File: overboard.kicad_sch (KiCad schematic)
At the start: 243 parts, among them J1 USB_C_Receptacle_USB2.0, J2 Trackpoint, K1 Key_Switch_LED, K10 Key_Switch_LED, K11 Key_Switch_LED, K12 Key_Switch_LED, K13 Key_Switch_LED, K14 Key_Switch_LED, K15 Key_Switch_LED, K16 Key_Switch_LED, K17 Key_Switch_LED, K18 Key_Switch_LED, K19 Key_Switch_LED, K2 Key_Switch_LED, K20 Key_Switch_LED, K21 Key_Switch_LED, K22 Key_Switch_LED, K23 Key_Switch_LED, K24 Key_Switch_LED, K25 Key_Switch_LED, K26 Key_Switch_LED, K27 Key_Switch_LED, K28 Key_Switch_LED, K29 Key_Switch_LED, K3 Key_Switch_LED, K30 Key_Switch_LED, K31 Key_Switch_LED, K32 Key_Switch_LED, K33 Key_Switch_LED, K34 Key_Switch_LED, K35 Key_Switch_LED, K36 Key_Switch_LED, K37 Key_Switch_LED, K38 Key_Switch_LED, K39 Key_Switch_LED, K4 Key_Switch_LED, K40 Key_Switch_LED, K41 Key_Switch_LED, K42 Key_Switch_LED, K43 Key_Switch_LED, K44 Key_Switch_LED, K45 Key_Switch_LED, K46 Key_Switch_LED, K47 Key_Switch_LED, K48 Key_Switch_LED, K49 Key_Switch, K5 Key_Switch_LED, K50 Key_Switch, K51 Key_Switch, K6 Key_Switch_LED, K7 Key_Switch_LED, K8 Key_Switch_LED, K9 Key_Switch_LED, Q1 Q_NMOS_DGS, Q2 Q_NPN_Darlington_BCE, Q3 Q_NPN_Darlington_BCE, SW1 SW_DIP_x04, SW2 RotaryEncoder_Switch, SW3 RotaryEncoder_Switch, SW4 SW_Push, U1 Teensy2.0++, U2 SKQUCAA010, U3 SKQUCAA010

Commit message: Changes
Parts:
- removed K1, K10, K11, K12, K13, K14, K15, K16, K17, K18, K19, K2, K20, K21, K22, K23, K24, K25, K26, K27, K28, K29, K3, K30, K31, K32, K33, K34, K35, K36, K37, K38, K39, K4, K40, K41, K42, K43, K44, K45, K46, K47, K48, K5, K6, K7, K8, K9: Key_Switch_LED, LED_THT:LED_D1.8mm_W3.3mm_H2.4mm, symbol MK:Key_Switch_LED
- removed SW1: SW_DIP_x04, Package_DIP:DIP-4_W10.16mm, symbol Switch:SW_DIP_x04
- added D49, D50, D51, D52, D53, D54, D55, D56, D57, D58, D59, D60, D61, D62, D63, D64, D65, D66, D67, D68, D69, D70, D71, D72, D73, D74, D75, D76, D77, D78, D79, D80, D81, D82, D83, D84, D85, D86, D87, D88, D89, D90, D91, D92, D93, D94, D95, D96: LED, LED_THT:LED_D1.8mm_W3.3mm_H2.4mm, symbol Device:LED
- added J1: Pimoroni_Trackball, Kicad-Footprints:pimoroni_trackball, symbol User:Pimoroni_Trackball
- added K1, K10, K11, K12, K13, K14, K15, K16, K17, K18, K19, K2, K20, K21, K22, K23, K24, K25, K26, K27, K28, K29, K3, K30, K31, K32, K33, K34, K35, K36, K37, K38, K39, K4, K40, K41, K42, K43, K44, K45, K46, K47, K48, K5, K6, K7, K8, K9: Key_Switch, Switch_Keyboard_Hotswap_Kailh:SW_Hotswap_Kailh_MX_1.00u, symbol MK:Key_Switch
- added S1, S2: DS04-254-1L-02BK, DS04-254-1L-02BK:SW_DS04-254-1L-02BK, symbol DS04-254-1L-02BK:DS04-254-1L-02BK
- C1: footprint Capacitor_THT:CP_Radial_Tantal_D4.5mm_P2.50mm -> Capacitor_THT:CP_Radial_D5.0mm_P2.00mm
- J3: renamed from J1; footprint LED_THT:LED_D1.8mm_W3.3mm_H2.4mm -> Connector_USB:USB_C_Receptacle_HRO_TYPE-C-31-M-12
- K49, K50, K51: footprint Switch_Keyboard_Hotswap_Kailh:SW_Hotswap_Kailh_MX_1.00u -> Button_Switch_Keyboard:SW_Cherry_MX_1.00u_PCB
- L1, L2: footprint Inductor_THT:L_Axial_L5.3mm_D2.2mm_P2.54mm_Vertical_Vishay_IM-1 -> Connector_JST:JST_PH_S2B-PH-SM4-TB_1x02-1MP_P2.00mm_Horizontal
- LCD1: footprint Keebio-Parts:Resistor -> Display_0xLib:OLED_I2C_128x64_0.96inch
- LS1, LS2: footprint Keebio-Parts:Resistor -> Buzzer_Beeper:Buzzer_Mallory_AST1109MLTRQ
- Q1, Q2, Q3: footprint Keebio-Parts:Resistor -> digikey-footprints:TO-220-3
- SW3: renamed from SW4; footprint Button_Switch_THT:SW_PUSH_6mm -> User:Bourns 7914H; symbol Switch:SW_Push -> Switch:SW_SPST
- renumbered D49 to D1, D58 to D10, D4 to D100, D5 to D101, D6 to D102, D7 to D103, D8 to D104, D9 to D105, D10 to D106, D11 to D107, D12 to D108, D13 to D109, D59 to D11, D14 to D110, D15 to D111, D16 to D112, D17 to D113, D18 to D114, D19 to D115, D20 to D116, D21 to D117, D22 to D118, D23 to D119, D60 to D12, D24 to D120, D25 to D121, D26 to D122, D27 to D123, D28 to D124, D29 to D125, D30 to D126, D31 to D127, D32 to D128, D33 to D129, D61 to D13, D34 to D130, D35 to D131, D36 to D132, D37 to D133, D38 to D134, D39 to D135, D40 to D136, D41 to D137, D42 to D138, D43 to D139, D62 to D14, D44 to D140, D45 to D141, D46 to D142, D47 to D143, D48 to D144, D99 to D145, D107 to D146, D102 to D147, D109 to D148, D97 to D149, D63 to D15, D98 to D150, D103 to D151, D104 to D152, D108 to D153, D100 to D154, D101 to D155, D105 to D156, D106 to D157, D110 to D158, D111 to D159, D64 to D16, D112 to D160, D113 to D161, D114 to D162, D115 to D163, D116 to D164, D117 to D165, D65 to D17, D66 to D18, D67 to D19, D50 to D2, D68 to D20, D69 to D21, D70 to D22, D71 to D23, D72 to D24, D73 to D25, D74 to D26, D75 to D27, D76 to D28, D77 to D29, D51 to D3, D78 to D30, D79 to D31, D80 to D32, D81 to D33, D82 to D34, D83 to D35, D84 to D36, D85 to D37, D86 to D38, D87 to D39, D52 to D4, D88 to D40, D89 to D41, D90 to D42, D91 to D43, D92 to D44, D93 to D45, D94 to D46, D95 to D47, D96 to D48, D53 to D5, D54 to D6, D55 to D7, D56 to D8, D57 to D9, D1 to D97, D2 to D98, D3 to D99, R15 to R1, R17 to R15, R18 to R16, R19 to R17, R20 to R18, R21 to R19, R16 to R2, R22 to R20, R23 to R21, R24 to R22, R25 to R23, R26 to R24, R27 to R25, R28 to R26, R29 to R27, R30 to R28, R31 to R29, R32 to R30, R33 to R31, R34 to R32, R35 to R33, R36 to R34, R37 to R35, R38 to R36, R39 to R37, R40 to R38, R41 to R39, R42 to R40, R43 to R41, R44 to R42, R45 to R43, R46 to R44, R47 to R45, R48 to R46, R49 to R47, R50 to R48, R51 to R49, R52 to R50, R55 to R51, R56 to R52, R57 to R53, R1 to R54, R2 to R55, R53 to R56, R54 to R57, SW2 to SW1, SW3 to SW2
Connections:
- net COL0: now also K1.1, K13.1, K25.1, K37.1
- net COL1: now also K14.1, K2.1, K26.1, K38.1
- net COL10: now also K19.1, K31.1, K43.1, K7.1
- net COL11: now also K20.1, K32.1, K44.1, K8.1
- net COL12: now also K21.1, K33.1, K45.1, K9.1
- net COL13: now also K10.1, K22.1, K34.1, K46.1
- net COL14: now also K11.1, K23.1, K35.1, K47.1
- net COL15: now also K12.1, K24.1, K36.1, K48.1
- net COL2: now also K15.1, K27.1, K3.1, K39.1
- net COL3: now also K16.1, K28.1, K4.1, K40.1
- net COL4: now also K17.1, K29.1, K41.1, K5.1
- net COL5: now also K18.1, K30.1, K42.1, K6.1
- net COL6: now also S1.1B, S1.2B, S2.1B, S2.2B; no longer U2.4 (Com)
- net COL7: now also K49.1, K50.1, K51.1, SW1.S1, SW2.S1
- net COL8: now also U2.4 (Com); no longer U3.4 (Com)
- net COL9: now also U3.4 (Com); no longer K49.1, K50.1, K51.1, SW1.S1, SW2.S1
- net GND: now also J1.5 (GND)
- net SCL: now also J1.3 (SCL)
- net SDA: now also J1.2 (SDA)
- net VCC: now also D49.2 (A), D50.2 (A), D51.2 (A), D52.2 (A), D53.2 (A), D54.2 (A), D55.2 (A), D56.2 (A), D57.2 (A), D58.2 (A), D59.2 (A), D60.2 (A), D61.2 (A), D62.2 (A), D63.2 (A), D64.2 (A), D65.2 (A), D66.2 (A), D67.2 (A), D68.2 (A), D69.2 (A), D70.2 (A), D71.2 (A), D72.2 (A), D73.2 (A), D74.2 (A), D75.2 (A), D76.2 (A), D77.2 (A), D78.2 (A), D79.2 (A), D80.2 (A), D81.2 (A), D82.2 (A), D83.2 (A), D84.2 (A), D85.2 (A), D86.2 (A), D87.2 (A), D88.2 (A), D89.2 (A), D90.2 (A), D91.2 (A), D92.2 (A), D93.2 (A), D94.2 (A), D95.2 (A), D96.2 (A), J1.1 (VCC)
- net at D8.2 (A): now also K8.2
- net at D25.2 (A): now also K25.2
- net at R41.1: now also D87.1 (K)
- net at R20.1: now also D66.1 (K)
- net at D47.2 (A): now also K47.2
- net at R3.1: now also D49.1 (K)
- net at D48.2 (A): now also K48.2
- net at R33.1: now also D79.1 (K)
- net at R11.1: now also D57.1 (K)
- net at D33.2 (A): now also K33.2
- net at R37.1: now also D83.1 (K)
- net at R26.1: now also D72.1 (K)
- net at R8.1: now also D54.1 (K)
- net at D28.2 (A): now also K28.2
- net at D1.2 (A): now also K1.2
- net at D42.2 (A): now also K42.2
- net at D5.2 (A): now also K5.2
- net at D15.2 (A): now also K15.2
- net at D40.2 (A): now also K40.2
- net at R36.1: now also D82.1 (K)
- net at D6.2 (A): now also K6.2
- net at R17.1: now also D63.1 (K)
- net at R34.1: now also D80.1 (K)
- net at D20.2 (A): now also K20.2
- net at D148.2 (A): now also S2.2A
- net at D39.2 (A): now also K39.2
- net at D17.2 (A): now also K17.2
- net at D11.2 (A): now also K11.2
- net at D4.2 (A): now also K4.2
- net at D7.2 (A): now also K7.2
- net at D32.2 (A): now also K32.2
- net at R24.1: now also D70.1 (K)
- net at D41.2 (A): now also K41.2
- net at R4.1: now also D50.1 (K)
- net at R10.1: now also D56.1 (K)
- net at D146.2 (A): now also S2.1A
- net at D24.2 (A): now also K24.2
- net at R7.1: now also D53.1 (K)
- net at D44.2 (A): now also K44.2
- net at R31.1: now also D77.1 (K)
- net at D43.2 (A): now also K43.2
- net at R45.1: now also D91.1 (K)
- net at D34.2 (A): now also K34.2
- net at R49.1: now also D95.1 (K)
- net at R39.1: now also D85.1 (K)
- net at R48.1: now also D94.1 (K)
- net at D36.2 (A): now also K36.2
- net at D18.2 (A): now also K18.2
- net at D31.2 (A): now also K31.2
- net at R21.1: now also D67.1 (K)
- net at R16.1: now also D62.1 (K)
- net at R40.1: now also D86.1 (K)
- net at D26.2 (A): now also K26.2
- net at D2.2 (A): now also K2.2
- net at R47.1: now also D93.1 (K)
- net at D12.2 (A): now also K12.2
- net at R43.1: now also D89.1 (K)
- net at D9.2 (A): now also K9.2
- net at R5.1: now also D51.1 (K)
- net at R14.1: now also D60.1 (K)
- net at D45.2 (A): now also K45.2
- net at D16.2 (A): now also K16.2
- net at R28.1: now also D74.1 (K)
- net at R6.1: now also D52.1 (K)
- net at R27.1: now also D73.1 (K)
- net at D19.2 (A): now also K19.2
- net at R44.1: now also D90.1 (K)
- net at D38.2 (A): now also K38.2
- net at R32.1: now also D78.1 (K)
- net at R38.1: now also D84.1 (K)
- net at D10.2 (A): now also K10.2
- net at R29.1: now also D75.1 (K)
- net at R19.1: now also D65.1 (K)
- net at D27.2 (A): now also K27.2
- net at D23.2 (A): now also K23.2
- net at D30.2 (A): now also K30.2
- net at R23.1: now also D69.1 (K)
- net at R35.1: now also D81.1 (K)
- net at R46.1: now also D92.1 (K)
- net at D21.2 (A): now also K21.2
- net at D14.2 (A): now also K14.2
- net at D37.2 (A): now also K37.2
- net at R22.1: now also D68.1 (K)
- net at D13.2 (A): now also K13.2
- net at D3.2 (A): now also K3.2
- net at D22.2 (A): now also K22.2
- net at R42.1: now also D88.1 (K)
- net at D35.2 (A): now also K35.2
- net at D46.2 (A): now also K46.2
- net at D29.2 (A): now also K29.2
- net at R13.1: now also D59.1 (K)
- net at R50.1: now also D96.1 (K)
- net at R15.1: now also D61.1 (K)
- net at D145.2 (A): now also S1.1A
- net at R30.1: now also D76.1 (K)
- net at R12.1: now also D58.1 (K)
- net at R9.1: now also D55.1 (K)
- net at D147.2 (A): now also S1.2A
- net at R25.1: now also D71.1 (K)
- net at R18.1: now also D64.1 (K)
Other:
- moved on the sheet: C1, D1, D10, D100, D101, D102, D103, D104, D105, D106, D107, D108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

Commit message: Add USB-C port
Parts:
- removed D145, D146, D147, D148, D149, D150, D151, D152, D153, D154, D155, D156, D157, D158: 1N4148, Diode_THT:D_DO-35_SOD27_P7.62mm_Horizontal, symbol Diode:1N4148
- removed D49, D50, D51, D52, D53, D54, D55, D56, D57, D61, D62, D63, D64, D65, D66, D67, D68, D69, D70, D71, D72, D73, D74, D75, D76, D77, D78, D79, D80, D81, D82, D83, D84, D85, D86, D87, D88, D89, D90, D91, D92, D93, D94, D95, D96: LED, LED_THT:LED_D1.8mm_W3.3mm_H2.4mm, symbol Device:LED
- removed J1: Pimoroni_Trackball, Kicad-Footprints:pimoroni_trackball, symbol User:Pimoroni_Trackball
- removed J3: USB_C_Receptacle_USB2.0, Connector_USB:USB_C_Receptacle_HRO_TYPE-C-31-M-12, symbol Connector:USB_C_Receptacle_USB2.0
- removed LS2: AST1109MLTRQ, Buzzer_Beeper:Buzzer_Mallory_AST1109MLTRQ, symbol AST1109MLTRQ:AST1109MLTRQ
- removed R10, R11, R15, R16, R17, R18, R19, R20, R21, R22, R23, R24, R25, R26, R27, R28, R29, R3, R30, R31, R32, R33, R34, R35, R36, R37, R38, R39, R4, R40, R41, R42, R43, R44, R45, R46, R47, R48, R49, R5, R50, R6, R7, R8, R9: 470, Keebio-Parts:Resistor, symbol Device:R_Small_US
- removed R54, R55: 5.1k, Keebio-Parts:Resistor, symbol Device:R_Small_US
- removed S1, S2: DS04-254-1L-02BK, DS04-254-1L-02BK:SW_DS04-254-1L-02BK, symbol DS04-254-1L-02BK:DS04-254-1L-02BK
- removed SW3: SW_Push, User:Bourns 7914H, symbol Switch:SW_SPST
- removed U2, U3: SKQUCAA010, Alps SKQUCAA010:SKQUCAA010, symbol Alps SKQUCAA010:SKQUCAA010
- added D60, D61, D62, D63, D64, D70, D71, D72, D73, D80, D81, D82, D83, D84: 1N4148, Diode_SMD:D_SOD-123, symbol Diode:1N4148
- added DIP1: DS04-254-1L-04BK, DS04-254-1L-04BK:SW_DS04-254-1L-04BK, symbol DS04-254-1L-04BK:DS04-254-1L-04BK
- added H1, H2, H3, H4: MountingHole, User:MountingHole_2.4mm_M2, symbol Mechanical:MountingHole
- added H5: MountingHole, User:Trackpoint_Mounting_Holes, symbol Mechanical:MountingHole
- added J1: USB_C_Receptacle_USB2.0, USB_Type-C:USB_C_Receptacle_HRO_TYPE-C-31-M-12, symbol Connector:USB_C_Receptacle_USB2.0
- added J2: Conn_01x04, symbol Connector_Generic:Conn_01x04
- added NAV1, NAV2: JOYSTICK_MINI, Sparkfun_Switches:JOYSTICK_MINI, symbol Sparkfun_Switches:JOYSTICK_MINI
- added R1, R2: 5.1k, Keebio-Parts:Resistor, symbol Device:R_Small_US
- added SW1: Reset_SW, truckpoint:CK_RKB2_Switch, symbol Switch:SW_Push
- C1: footprint Capacitor_THT:CP_Radial_D5.0mm_P2.00mm -> Capacitor_THT:C_Radial_D4.0mm_H7.0mm_P1.50mm
- D00: renamed from D1; footprint Diode_THT:D_DO-35_SOD27_P7.62mm_Horizontal -> User:Diode_THT
- D01: renamed from D13; footprint Diode_THT:D_DO-35_SOD27_P7.62mm_Horizontal -> User:Diode_THT
- D02: renamed from D25; footprint Diode_THT:D_DO-35_SOD27_P7.62mm_Horizontal -> User:Diode_THT
- D03: renamed from D37; footprint Diode_THT:D_DO-35_SOD27_P7.62mm_Horizontal -> User:Diode_THT
- D10: renamed from D2; footprint Diode_THT:D_DO-35_SOD27_P7.62mm_Horizontal -> User:Diode_THT
- D11: renamed from D14; footprint Diode_THT:D_DO-35_SOD27_P7.62mm_Horizontal -> User:Diode_THT
- D12: renamed from D26; footprint Diode_THT:D_DO-35_SOD27_P7.62mm_Horizontal -> User:Diode_THT
- D13: renamed from D38; footprint Diode_THT:D_DO-35_SOD27_P7.62mm_Horizontal -> User:Diode_THT
- D20: renamed from D3; footprint Diode_THT:D_DO-35_SOD27_P7.62mm_Horizontal -> User:Diode_THT
- D21: renamed from D15; footprint Diode_THT:D_DO-35_SOD27_P7.62mm_Horizontal -> User:Diode_THT
- D22: renamed from D27; footprint Diode_THT:D_DO-35_SOD27_P7.62mm_Horizontal -> User:Diode_THT
- D23: renamed from D39; footprint Diode_THT:D_DO-35_SOD27_P7.62mm_Horizontal -> User:Diode_THT
- D30: renamed from D4; footprint Diode_THT:D_DO-35_SOD27_P7.62mm_Horizontal -> User:Diode_THT
- D31: renamed from D16; footprint Diode_THT:D_DO-35_SOD27_P7.62mm_Horizontal -> User:Diode_THT
- D32: renamed from D28; footprint Diode_THT:D_DO-35_SOD27_P7.62mm_Horizontal -> User:Diode_THT
- D33: renamed from D40; footprint Diode_THT:D_DO-35_SOD27_P7.62mm_Horizontal -> User:Diode_THT
- D40: renamed from D5; footprint Diode_THT:D_DO-35_SOD27_P7.62mm_Horizontal -> User:Diode_THT
- D41: renamed from D17; footprint Diode_THT:D_DO-35_SOD27_P7.62mm_Horizontal -> User:Diode_THT
- D42: renamed from D29; footprint Diode_THT:D_DO-35_SOD27_P7.62mm_Horizontal -> User:Diode_THT
- D43: renamed from D41; footprint Diode_THT:D_DO-35_SOD27_P7.62mm_Horizontal -> User:Diode_THT
- D50: renamed from D6; footprint Diode_THT:D_DO-35_SOD27_P7.62mm_Horizontal -> User:Diode_THT
- D51: renamed from D18; footprint Diode_THT:D_DO-35_SOD27_P7.62mm_Horizontal -> User:Diode_THT
- D52: renamed from D30; footprint Diode_THT:D_DO-35_SOD27_P7.62mm_Horizontal -> User:Diode_THT
- D53: renamed from D42; footprint Diode_THT:D_DO-35_SOD27_P7.62mm_Horizontal -> User:Diode_THT
- D90: renamed from D161; footprint Diode_THT:D_DO-35_SOD27_P7.62mm_Horizontal -> User:Diode_THT
- D91: renamed from D162; footprint Diode_THT:D_DO-35_SOD27_P7.62mm_Horizontal -> User:Diode_THT
- D92: renamed from D163; footprint Diode_THT:D_DO-35_SOD27_P7.62mm_Horizontal -> User:Diode_THT
- D93: renamed from D164; footprint Diode_THT:D_DO-35_SOD27_P7.62mm_Horizontal -> User:Diode_THT
- D94: renamed from D165; footprint Diode_THT:D_DO-35_SOD27_P7.62mm_Horizontal -> User:Diode_THT
- DA0: renamed from D7; footprint Diode_THT:D_DO-35_SOD27_P7.62mm_Horizontal -> User:Diode_THT
- DA1: renamed from D19; footprint Diode_THT:D_DO-35_SOD27_P7.62mm_Horizontal -> User:Diode_THT
- DA2: renamed from D31; footprint Diode_THT:D_DO-35_SOD27_P7.62mm_Horizontal -> User:Diode_THT
- DA3: renamed from D43; footprint Diode_THT:D_DO-35_SOD27_P7.62mm_Horizontal -> User:Diode_THT
- DB0: renamed from D8; footprint Diode_THT:D_DO-35_SOD27_P7.62mm_Horizontal -> User:Diode_THT
- DB1: renamed from D20; footprint Diode_THT:D_DO-35_SOD27_P7.62mm_Horizontal -> User:Diode_THT
- DB2: renamed from D32; footprint Diode_THT:D_DO-35_SOD27_P7.62mm_Horizontal -> User:Diode_THT
- DB3: renamed from D44; footprint Diode_THT:D_DO-35_SOD27_P7.62mm_Horizontal -> User:Diode_THT
- DC0: renamed from D9; footprint Diode_THT:D_DO-35_SOD27_P7.62mm_Horizontal -> User:Diode_THT
- DC1: renamed from D21; footprint Diode_THT:D_DO-35_SOD27_P7.62mm_Horizontal -> User:Diode_THT
- DC2: renamed from D33; footprint Diode_THT:D_DO-35_SOD27_P7.62mm_Horizontal -> User:Diode_THT
- DC3: renamed from D45; footprint Diode_THT:D_DO-35_SOD27_P7.62mm_Horizontal -> User:Diode_THT
- DD0: renamed from D10; footprint Diode_THT:D_DO-35_SOD27_P7.62mm_Horizontal -> User:Diode_THT
- DD1: renamed from D22; footprint Diode_THT:D_DO-35_SOD27_P7.62mm_Horizontal -> User:Diode_THT
- DD2: renamed from D34; footprint Diode_THT:D_DO-35_SOD27_P7.62mm_Horizontal -> User:Diode_THT
- DD3: renamed from D46; footprint Diode_THT:D_DO-35_SOD27_P7.62mm_Horizontal -> User:Diode_THT
- DE0: renamed from D11; footprint Diode_THT:D_DO-35_SOD27_P7.62mm_Horizontal -> User:Diode_THT
- DE1: renamed from D23; footprint Diode_THT:D_DO-35_SOD27_P7.62mm_Horizontal -> User:Diode_THT
- DE2: renamed from D35; footprint Diode_THT:D_DO-35_SOD27_P7.62mm_Horizontal -> User:Diode_THT
- DE3: renamed from D47; footprint Diode_THT:D_DO-35_SOD27_P7.62mm_Horizontal -> User:Diode_THT
- DF0: renamed from D12; footprint Diode_THT:D_DO-35_SOD27_P7.62mm_Horizontal -> User:Diode_THT
- DF1: renamed from D24; footprint Diode_THT:D_DO-35_SOD27_P7.62mm_Horizontal -> User:Diode_THT
- DF2: renamed from D36; footprint Diode_THT:D_DO-35_SOD27_P7.62mm_Horizontal -> User:Diode_THT
- DF3: renamed from D48; footprint Diode_THT:D_DO-35_SOD27_P7.62mm_Horizontal -> User:Diode_THT
- DL1: renamed from D159; footprint Diode_THT:D_DO-41_SOD81_P10.16mm_Horizontal -> Diode_THT:D_DO-41_SOD81_P7.62mm_Horizontal
- DL2: renamed from D160; footprint Diode_THT:D_DO-41_SOD81_P10.16mm_Horizontal -> Diode_THT:D_DO-41_SOD81_P7.62mm_Horizontal
- ENC1: renamed from SW1; footprint Encoder:RollerEncoder_Panasonic_EVQWGD001 -> User:Panasonic_EVQ-WGD001_LargerCutout
- ENC2: renamed from SW2; footprint Encoder:RollerEncoder_Panasonic_EVQWGD001 -> User:Panasonic_EVQ-WGD001_LargerCutout
- J3: renamed from J2; footprint pierce:TRACKPOINT -> Connector_PinHeader_2.54mm:PinHeader_1x05_P2.54mm_Vertical
- K00: renamed from K1; footprint Switch_Keyboard_Hotswap_Kailh:SW_Hotswap_Kailh_MX_1.00u -> MK_Switches:MXOnly-1U-NoLED
- K01: renamed from K13; footprint Switch_Keyboard_Hotswap_Kailh:SW_Hotswap_Kailh_MX_1.00u -> MK_Switches:MXOnly-1U-NoLED
- K02: renamed from K25; footprint Switch_Keyboard_Hotswap_Kailh:SW_Hotswap_Kailh_MX_1.00u -> MK_Switches:MXOnly-1U-NoLED
- K03: renamed from K37; footprint Switch_Keyboard_Hotswap_Kailh:SW_Hotswap_Kailh_MX_1.00u -> MK_Switches:MXOnly-1U-NoLED
- K10: renamed from K2; footprint Switch_Keyboard_Hotswap_Kailh:SW_Hotswap_Kailh_MX_1.00u -> MK_Switches:MXOnly-1U-NoLED
- K11: renamed from K14; footprint Switch_Keyboard_Hotswap_Kailh:SW_Hotswap_Kailh_MX_1.00u -> MK_Switches:MXOnly-1U-NoLED
- K12: renamed from K26; footprint Switch_Keyboard_Hotswap_Kailh:SW_Hotswap_Kailh_MX_1.00u -> MK_Switches:MXOnly-1U-NoLED
- K13: renamed from K38; footprint Switch_Keyboard_Hotswap_Kailh:SW_Hotswap_Kailh_MX_1.00u -> MK_Switches:MXOnly-1U-NoLED
- K20: renamed from K3; footprint Switch_Keyboard_Hotswap_Kailh:SW_Hotswap_Kailh_MX_1.00u -> MK_Switches:MXOnly-1U-NoLED
- K21: renamed from K15; footprint Switch_Keyboard_Hotswap_Kailh:SW_Hotswap_Kailh_MX_1.00u -> MK_Switches:MXOnly-1U-NoLED
- K22: renamed from K27; footprint Switch_Keyboard_Hotswap_Kailh:SW_Hotswap_Kailh_MX_1.00u -> MK_Switches:MXOnly-1U-NoLED
- K23: renamed from K39; footprint Switch_Keyboard_Hotswap_Kailh:SW_Hotswap_Kailh_MX_1.00u -> MK_Switches:MXOnly-1U-NoLED
- K30: renamed from K4; footprint Switch_Keyboard_Hotswap_Kailh:SW_Hotswap_Kailh_MX_1.00u -> MK_Switches:MXOnly-1U-NoLED
- K31: renamed from K16; footprint Switch_Keyboard_Hotswap_Kailh:SW_Hotswap_Kailh_MX_1.00u -> MK_Switches:MXOnly-1U-NoLED
- K32: renamed from K28; footprint Switch_Keyboard_Hotswap_Kailh:SW_Hotswap_Kailh_MX_1.00u -> MK_Switches:MXOnly-1U-NoLED
- K33: renamed from K40; footprint Switch_Keyboard_Hotswap_Kailh:SW_Hotswap_Kailh_MX_1.00u -> MK_Switches:MXOnly-1U-NoLED
- K40: renamed from K5; footprint Switch_Keyboard_Hotswap_Kailh:SW_Hotswap_Kailh_MX_1.00u -> MK_Switches:MXOnly-1U-NoLED
- K41: renamed from K17; footprint Switch_Keyboard_Hotswap_Kailh:SW_Hotswap_Kailh_MX_1.00u -> MK_Switches:MXOnly-1U-NoLED
- K42: renamed from K29; footprint Switch_Keyboard_Hotswap_Kailh:SW_Hotswap_Kailh_MX_1.00u -> MK_Switches:MXOnly-1U-NoLED
- K43: renamed from K41; footprint Switch_Keyboard_Hotswap_Kailh:SW_Hotswap_Kailh_MX_1.00u -> MK_Switches:MXOnly-1U-NoLED
- K50: renamed from K6; footprint Switch_Keyboard_Hotswap_Kailh:SW_Hotswap_Kailh_MX_1.00u -> MK_Switches:MXOnly-1U-NoLED
- K51: renamed from K18; footprint Switch_Keyboard_Hotswap_Kailh:SW_Hotswap_Kailh_MX_1.00u -> MK_Switches:MXOnly-1U-NoLED
- K52: renamed from K30; footprint Switch_Keyboard_Hotswap_Kailh:SW_Hotswap_Kailh_MX_1.00u -> MK_Switches:MXOnly-1U-NoLED
- K53: renamed from K42; footprint Switch_Keyboard_Hotswap_Kailh:SW_Hotswap_Kailh_MX_1.00u -> MK_Switches:MXOnly-1U-NoLED
- K92: renamed from K49; footprint Button_Switch_Keyboard:SW_Cherry_MX_1.00u_PCB -> MK_Switches:MXOnly-1U-NoLED
- K93: renamed from K50; footprint Button_Switch_Keyboard:SW_Cherry_MX_1.00u_PCB -> MK_Switches:MXOnly-1U-NoLED
- K94: renamed from K51; footprint Button_Switch_Keyboard:SW_Cherry_MX_1.00u_PCB -> MK_Switches:MXOnly-1U-NoLED
- KA0: renamed from K7; footprint Switch_Keyboard_Hotswap_Kailh:SW_Hotswap_Kailh_MX_1.00u -> MK_Switches:MXOnly-1U-NoLED
- KA1: renamed from K19; footprint Switch_Keyboard_Hotswap_Kailh:SW_Hotswap_Kailh_MX_1.00u -> MK_Switches:MXOnly-1U-NoLED
- KA2: renamed from K31; footprint Switch_Keyboard_Hotswap_Kailh:SW_Hotswap_Kailh_MX_1.00u -> MK_Switches:MXOnly-1U-NoLED
- KA3: renamed from K43; footprint Switch_Keyboard_Hotswap_Kailh:SW_Hotswap_Kailh_MX_1.00u -> MK_Switches:MXOnly-1U-NoLED
- KB0: renamed from K8; footprint Switch_Keyboard_Hotswap_Kailh:SW_Hotswap_Kailh_MX_1.00u -> MK_Switches:MXOnly-1U-NoLED
- KB1: renamed from K20; footprint Switch_Keyboard_Hotswap_Kailh:SW_Hotswap_Kailh_MX_1.00u -> MK_Switches:MXOnly-1U-NoLED
- KB2: renamed from K32; footprint Switch_Keyboard_Hotswap_Kailh:SW_Hotswap_Kailh_MX_1.00u -> MK_Switches:MXOnly-1U-NoLED
- KB3: renamed from K44; footprint Switch_Keyboard_Hotswap_Kailh:SW_Hotswap_Kailh_MX_1.00u -> MK_Switches:MXOnly-1U-NoLED
- KC0: renamed from K9; footprint Switch_Keyboard_Hotswap_Kailh:SW_Hotswap_Kailh_MX_1.00u -> MK_Switches:MXOnly-1U-NoLED
- KC1: renamed from K21; footprint Switch_Keyboard_Hotswap_Kailh:SW_Hotswap_Kailh_MX_1.00u -> MK_Switches:MXOnly-1U-NoLED
- KC2: renamed from K33; footprint Switch_Keyboard_Hotswap_Kailh:SW_Hotswap_Kailh_MX_1.00u -> MK_Switches:MXOnly-1U-NoLED
- KC3: renamed from K45; footprint Switch_Keyboard_Hotswap_Kailh:SW_Hotswap_Kailh_MX_1.00u -> MK_Switches:MXOnly-1U-NoLED
- KD0: renamed from K10; footprint Switch_Keyboard_Hotswap_Kailh:SW_Hotswap_Kailh_MX_1.00u -> MK_Switches:MXOnly-1U-NoLED
- KD1: renamed from K22; footprint Switch_Keyboard_Hotswap_Kailh:SW_Hotswap_Kailh_MX_1.00u -> MK_Switches:MXOnly-1U-NoLED
- KD2: renamed from K34; footprint Switch_Keyboard_Hotswap_Kailh:SW_Hotswap_Kailh_MX_1.00u -> MK_Switches:MXOnly-1U-NoLED
- KD3: renamed from K46; footprint Switch_Keyboard_Hotswap_Kailh:SW_Hotswap_Kailh_MX_1.00u -> MK_Switches:MXOnly-1U-NoLED
- KE0: renamed from K11; footprint Switch_Keyboard_Hotswap_Kailh:SW_Hotswap_Kailh_MX_1.00u -> MK_Switches:MXOnly-1U-NoLED
- KE1: renamed from K23; footprint Switch_Keyboard_Hotswap_Kailh:SW_Hotswap_Kailh_MX_1.00u -> MK_Switches:MXOnly-1U-NoLED
- KE2: renamed from K35; footprint Switch_Keyboard_Hotswap_Kailh:SW_Hotswap_Kailh_MX_1.00u -> MK_Switches:MXOnly-1U-NoLED
- KE3: renamed from K47; footprint Switch_Keyboard_Hotswap_Kailh:SW_Hotswap_Kailh_MX_1.00u -> MK_Switches:MXOnly-1U-NoLED
- KF0: renamed from K12; footprint Switch_Keyboard_Hotswap_Kailh:SW_Hotswap_Kailh_MX_1.00u -> MK_Switches:MXOnly-1U-NoLED
- KF1: renamed from K24; footprint Switch_Keyboard_Hotswap_Kailh:SW_Hotswap_Kailh_MX_1.00u -> MK_Switches:MXOnly-1U-NoLED
- KF2: renamed from K36; footprint Switch_Keyboard_Hotswap_Kailh:SW_Hotswap_Kailh_MX_1.00u -> MK_Switches:MXOnly-1U-NoLED
- KF3: renamed from K48; footprint Switch_Keyboard_Hotswap_Kailh:SW_Hotswap_Kailh_MX_1.00u -> MK_Switches:MXOnly-1U-NoLED
- L1, L2: footprint Connector_JST:JST_PH_S2B-PH-SM4-TB_1x02-1MP_P2.00mm_Horizontal -> Connector_JST:JST_PH_S2B-PH-K_1x02_P2.00mm_Horizontal
- RGB1: renamed from D97; footprint LED_SMD_0xLib:LED_SK6812MINI-E_3.2x2.8mm -> User:SK6812MINI-E_RGB_LED_3.2x2.8mm
- RGB10: renamed from D111; footprint LED_SMD_0xLib:LED_SK6812MINI-E_3.2x2.8mm -> User:SK6812MINI-E_RGB_LED_3.2x2.8mm
- RGB11: renamed from D110; footprint LED_SMD_0xLib:LED_SK6812MINI-E_3.2x2.8mm -> User:SK6812MINI-E_RGB_LED_3.2x2.8mm
- RGB12: renamed from D109; footprint LED_SMD_0xLib:LED_SK6812MINI-E_3.2x2.8mm -> User:SK6812MINI-E_RGB_LED_3.2x2.8mm
- RGB13: renamed from D108; footprint LED_SMD_0xLib:LED_SK6812MINI-E_3.2x2.8mm -> User:SK6812MINI-E_RGB_LED_3.2x2.8mm
- RGB14: renamed from D107; footprint LED_SMD_0xLib:LED_SK6812MINI-E_3.2x2.8mm -> User:SK6812MINI-E_RGB_LED_3.2x2.8mm
- RGB15: renamed from D106; footprint LED_SMD_0xLib:LED_SK6812MINI-E_3.2x2.8mm -> User:SK6812MINI-E_RGB_LED_3.2x2.8mm
- RGB16: renamed from D105; footprint LED_SMD_0xLib:LED_SK6812MINI-E_3.2x2.8mm -> User:SK6812MINI-E_RGB_LED_3.2x2.8mm
- RGB17: renamed from D113; footprint LED_SMD_0xLib:LED_SK6812MINI-E_3.2x2.8mm -> User:SK6812MINI-E_RGB_LED_3.2x2.8mm
- RGB18: renamed from D114; footprint LED_SMD_0xLib:LED_SK6812MINI-E_3.2x2.8mm -> User:SK6812MINI-E_RGB_LED_3.2x2.8mm
- RGB19: renamed from D115; footprint LED_SMD_0xLib:LED_SK6812MINI-E_3.2x2.8mm -> User:SK6812MINI-E_RGB_LED_3.2x2.8mm
- RGB2: renamed from D98; footprint LED_SMD_0xLib:LED_SK6812MINI-E_3.2x2.8mm -> User:SK6812MINI-E_RGB_LED_3.2x2.8mm
- RGB20: renamed from D116; footprint LED_SMD_0xLib:LED_SK6812MINI-E_3.2x2.8mm -> User:SK6812MINI-E_RGB_LED_3.2x2.8mm
- RGB21: renamed from D117; footprint LED_SMD_0xLib:LED_SK6812MINI-E_3.2x2.8mm -> User:SK6812MINI-E_RGB_LED_3.2x2.8mm
- RGB22: renamed from D118; footprint LED_SMD_0xLib:LED_SK6812MINI-E_3.2x2.8mm -> User:SK6812MINI-E_RGB_LED_3.2x2.8mm
- RGB23: renamed from D119; footprint LED_SMD_0xLib:LED_SK6812MINI-E_3.2x2.8mm -> User:SK6812MINI-E_RGB_LED_3.2x2.8mm
- RGB24: renamed from D120; footprint LED_SMD_0xLib:LED_SK6812MINI-E_3.2x2.8mm -> User:SK6812MINI-E_RGB_LED_3.2x2.8mm
- RGB25: renamed from D128; footprint LED_SMD_0xLib:LED_SK6812MINI-E_3.2x2.8mm -> User:SK6812MINI-E_RGB_LED_3.2x2.8mm
- RGB26: renamed from D127; footprint LED_SMD_0xLib:LED_SK6812MINI-E_3.2x2.8mm -> User:SK6812MINI-E_RGB_LED_3.2x2.8mm
- RGB27: renamed from D126; footprint LED_SMD_0xLib:LED_SK6812MINI-E_3.2x2.8mm -> User:SK6812MINI-E_RGB_LED_3.2x2.8mm
- RGB28: renamed from D125; footprint LED_SMD_0xLib:LED_SK6812MINI-E_3.2x2.8mm -> User:SK6812MINI-E_RGB_LED_3.2x2.8mm
- RGB29: renamed from D124; footprint LED_SMD_0xLib:LED_SK6812MINI-E_3.2x2.8mm -> User:SK6812MINI-E_RGB_LED_3.2x2.8mm
- RGB3: renamed from D99; footprint LED_SMD_0xLib:LED_SK6812MINI-E_3.2x2.8mm -> User:SK6812MINI-E_RGB_LED_3.2x2.8mm
- RGB30: renamed from D123; footprint LED_SMD_0xLib:LED_SK6812MINI-E_3.2x2.8mm -> User:SK6812MINI-E_RGB_LED_3.2x2.8mm
- RGB31: renamed from D122; footprint LED_SMD_0xLib:LED_SK6812MINI-E_3.2x2.8mm -> User:SK6812MINI-E_RGB_LED_3.2x2.8mm
- RGB32: renamed from D121; footprint LED_SMD_0xLib:LED_SK6812MINI-E_3.2x2.8mm -> User:SK6812MINI-E_RGB_LED_3.2x2.8mm
- RGB33: renamed from D129; footprint LED_SMD_0xLib:LED_SK6812MINI-E_3.2x2.8mm -> User:SK6812MINI-E_RGB_LED_3.2x2.8mm
- RGB34: renamed from D130; footprint LED_SMD_0xLib:LED_SK6812MINI-E_3.2x2.8mm -> User:SK6812MINI-E_RGB_LED_3.2x2.8mm
- RGB35: renamed from D131; footprint LED_SMD_0xLib:LED_SK6812MINI-E_3.2x2.8mm -> User:SK6812MINI-E_RGB_LED_3.2x2.8mm
- RGB36: renamed from D132; footprint LED_SMD_0xLib:LED_SK6812MINI-E_3.2x2.8mm -> User:SK6812MINI-E_RGB_LED_3.2x2.8mm
- RGB37: renamed from D133; footprint LED_SMD_0xLib:LED_SK6812MINI-E_3.2x2.8mm -> User:SK6812MINI-E_RGB_LED_3.2x2.8mm
- RGB38: renamed from D134; footprint LED_SMD_0xLib:LED_SK6812MINI-E_3.2x2.8mm -> User:SK6812MINI-E_RGB_LED_3.2x2.8mm
- RGB39: renamed from D135; footprint LED_SMD_0xLib:LED_SK6812MINI-E_3.2x2.8mm -> User:SK6812MINI-E_RGB_LED_3.2x2.8mm
- RGB4: renamed from D100; footprint LED_SMD_0xLib:LED_SK6812MINI-E_3.2x2.8mm -> User:SK6812MINI-E_RGB_LED_3.2x2.8mm
- RGB40: renamed from D136; footprint LED_SMD_0xLib:LED_SK6812MINI-E_3.2x2.8mm -> User:SK6812MINI-E_RGB_LED_3.2x2.8mm
- RGB41: renamed from D144; footprint LED_SMD_0xLib:LED_SK6812MINI-E_3.2x2.8mm -> User:SK6812MINI-E_RGB_LED_3.2x2.8mm
- RGB42: renamed from D143; footprint LED_SMD_0xLib:LED_SK6812MINI-E_3.2x2.8mm -> User:SK6812MINI-E_RGB_LED_3.2x2.8mm
- RGB43: renamed from D142; footprint LED_SMD_0xLib:LED_SK6812MINI-E_3.2x2.8mm -> User:SK6812MINI-E_RGB_LED_3.2x2.8mm
- RGB44: renamed from D141; footprint LED_SMD_0xLib:LED_SK6812MINI-E_3.2x2.8mm -> User:SK6812MINI-E_RGB_LED_3.2x2.8mm
- RGB45: renamed from D140; footprint LED_SMD_0xLib:LED_SK6812MINI-E_3.2x2.8mm -> User:SK6812MINI-E_RGB_LED_3.2x2.8mm
- RGB46: renamed from D139; footprint LED_SMD_0xLib:LED_SK6812MINI-E_3.2x2.8mm -> User:SK6812MINI-E_RGB_LED_3.2x2.8mm
- RGB47: renamed from D138; footprint LED_SMD_0xLib:LED_SK6812MINI-E_3.2x2.8mm -> User:SK6812MINI-E_RGB_LED_3.2x2.8mm
- RGB48: renamed from D137; footprint LED_SMD_0xLib:LED_SK6812MINI-E_3.2x2.8mm -> User:SK6812MINI-E_RGB_LED_3.2x2.8mm
- renumbered D58 to LED1, D59 to LED2, D60 to LED3, LCD1 to OLED1, Q2 to Q1, Q3 to Q2, Q1 to Q3, R14 to R10, R13 to R11, R51 to R3, R53 to R4, R52 to R5, R56 to R6, R57 to R7, R1 to R8, R2 to R9
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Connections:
- net AUDIO: now also U1.19 (PC6_OC3A); no longer U1.17 (PC4_OC3C)
- net BACKLIGHT: now also U1.18 (PC5_OC3B); no longer U1.19 (PC6_OC3A)
- net COL0: no longer U1.41 (PB5_OC1A)
- net COL1: no longer U1.40 (PB4_OC2A)
- net COL2: no longer U1.39 (PB3_MISO)
- net COL3: no longer U1.38 (PB2_MOSI)
- net COL4: no longer U1.37 (PB1_SCLK)
- net COL5: no longer U1.36 (PB0_SS)
- net COL6: now also NAV1.GND; no longer U1.35 (PE7_INT7_AIN1)
- net COL7: now also DIP1.1A, DIP1.2A, DIP1.3A, DIP1.4A; no longer ENC1.S1, ENC2.S1, K92.1, K93.1, K94.1, U1.34 (PE6_INT6_AIN0)
- net COL8: now also NAV2.GND; no longer U1.31 (PF0_ADC0)
- net COL9: now also ENC1.S1, ENC2.S1, K92.1, K93.1, K94.1; no longer U1.30 (PF1_ADC1)
- net D+: now also J1.A6 (D+), J1.B6 (D+), J2.3 (Pin_3)
- net D-: now also J1.A7 (D-), J1.B7 (D-), J2.2 (Pin_2)
- net ENC_A: no longer U1.14 (PC1)
- net ENC_B1: no longer U1.15 (PC2)
- net ENC_B2: no longer U1.16 (PC3_T3)
- net GND: now also J1.A1 (GND), J1.A12 (GND), J1.B1 (GND), J1.B12 (GND), J1.S1 (SHIELD), J2.4 (Pin_4), R1.1, R2.1, SW1.1
- net RGB_DI: now also U1.42 (PB6_OC1B); no longer U1.20 (PC7_ICP3)
- net ROW0: now also D60.1 (K), D70.1 (K), D80.1 (K); no longer U1.9 (PD6_T1_LED)
- net ROW1: now also D61.1 (K), D71.1 (K), D81.1 (K); no longer U1.10 (PD7_T0)
- net ROW2: now also D62.1 (K), D72.1 (K), D82.1 (K); no longer U1.11 (PE0)
- net ROW3: now also D63.1 (K), D73.1 (K), D83.1 (K); no longer U1.12 (PE1)
- net ROW4: now also D64.1 (K), D84.1 (K); no longer U1.13 (PC0)
- net RST: now also SW1.2
- net SOLENOID2: now also U1.17 (PC4_OC3C); no longer U1.18 (PC5_OC3B)
- net AUDIO_ALT renamed SOLENOID1
- net SOLENOID1: now also R6.1
- net COL10 renamed COLA
- net COLA: no longer U1.29 (PF2_ADC2)
- net COL11 renamed COLB
- net COLB: no longer U1.28 (PF3_ADC3)
- net COL12 renamed COLC
- net COLC: no longer U1.27 (PF4_ADC4)
- net COL13 renamed COLD
- net COLD: no longer U1.26 (PF5_ADC5)
- net COL14 renamed COLE
- net COLE: no longer U1.25 (PF6_ADC6)
- net COL15 renamed COLF
- net COLF: no longer U1.24 (PF7_ADC7)
- removed net SOLENOID: R6.1, U1.42 (PB6_OC1B)
- new net: D61.2 (A), NAV1.C (LEFT)
- new net: D70.2 (A), DIP1.1B
- new net: D71.2 (A), DIP1.2B
- new net: D72.2 (A), DIP1.3B
- new net: D73.2 (A), DIP1.4B
- new net: D80.2 (A), NAV2.A (UP)
- new net: D83.2 (A), NAV2.B (RIGHT)
- new net: D81.2 (A), NAV2.C (LEFT)
- new net: D82.2 (A), NAV2.CTR (CENT)
- new net: D84.2 (A), NAV2.D (DOWN)
- new net: D62.2 (A), NAV1.CTR (CENT)
- new net: J1.B5 (CC2), R2.2
- new net: D64.2 (A), NAV1.D (DOWN)
- new net: D60.2 (A), NAV1.A (UP)
- new net: J1.A5 (CC1), R1.2
- new net: D63.2 (A), NAV1.B (RIGHT)
- new net VBUS: J1.A4 (VBUS), J1.A9 (VBUS), J1.B4 (VBUS), J1.B9 (VBUS), J2.1 (Pin_1)
- no-connect marks 0 -> 2
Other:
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
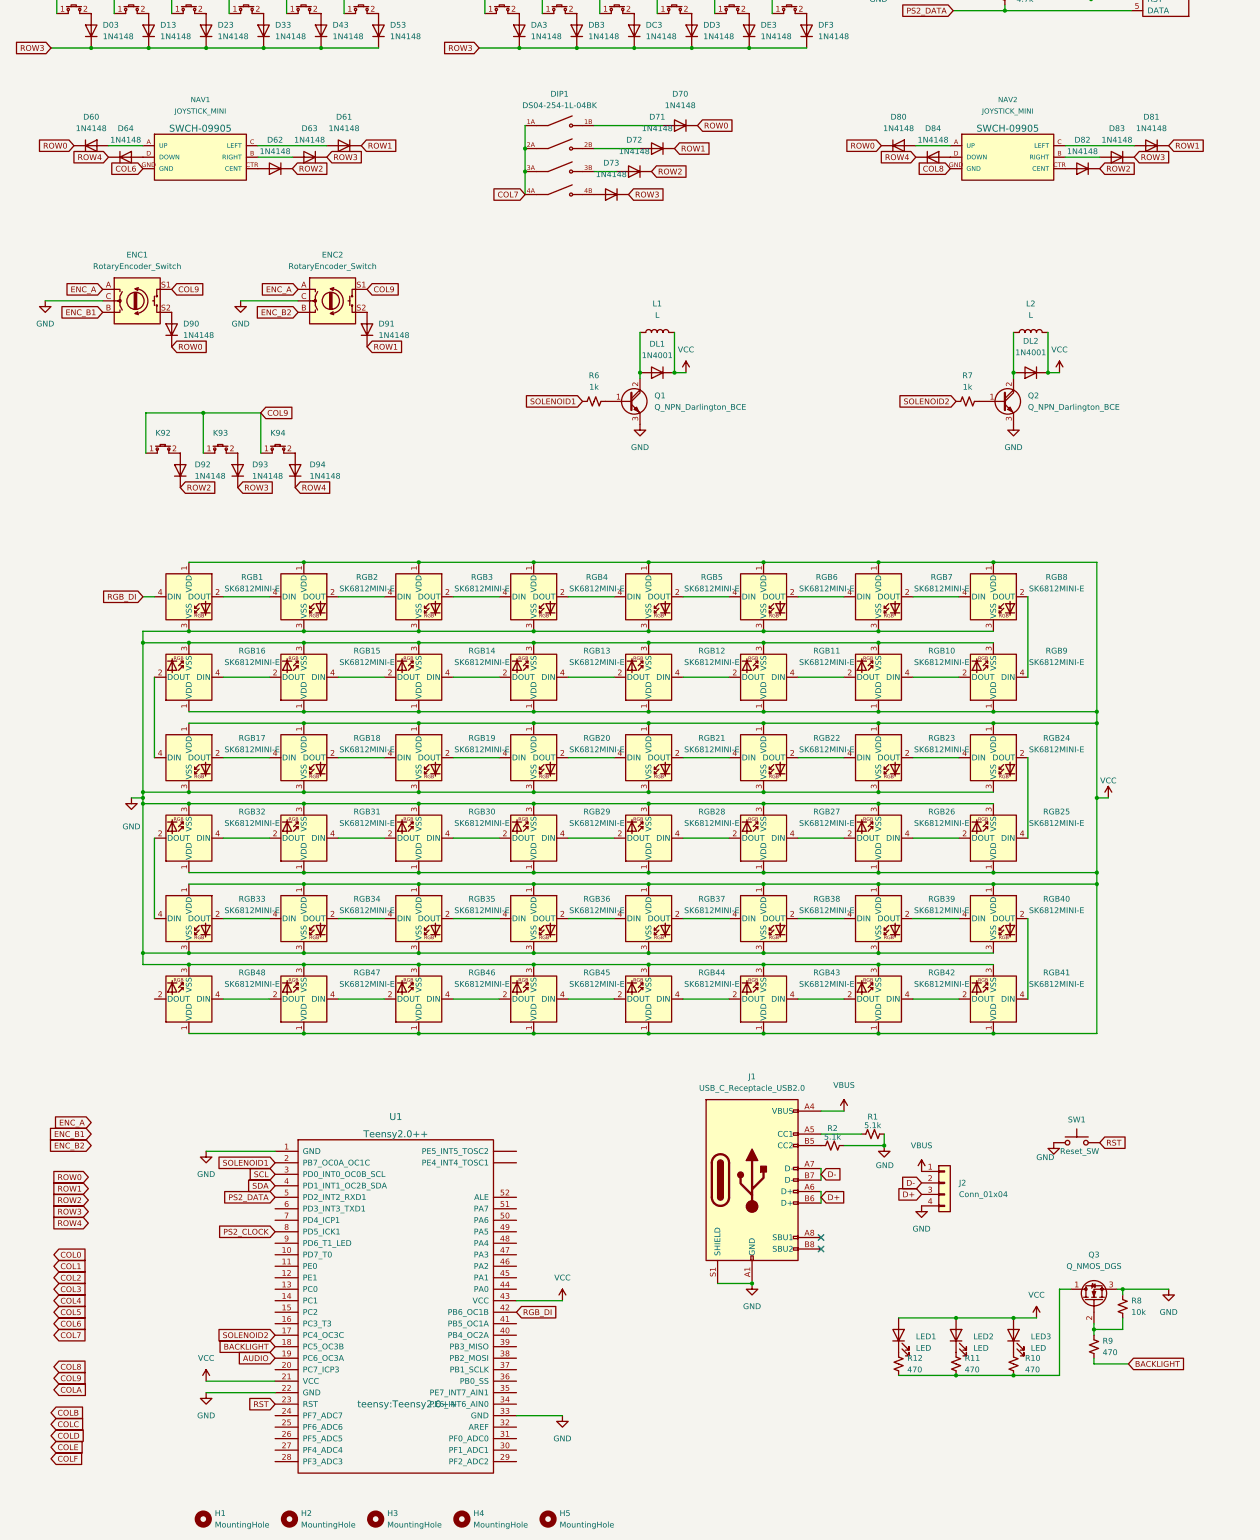
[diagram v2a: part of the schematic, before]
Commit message: 48 switch layout
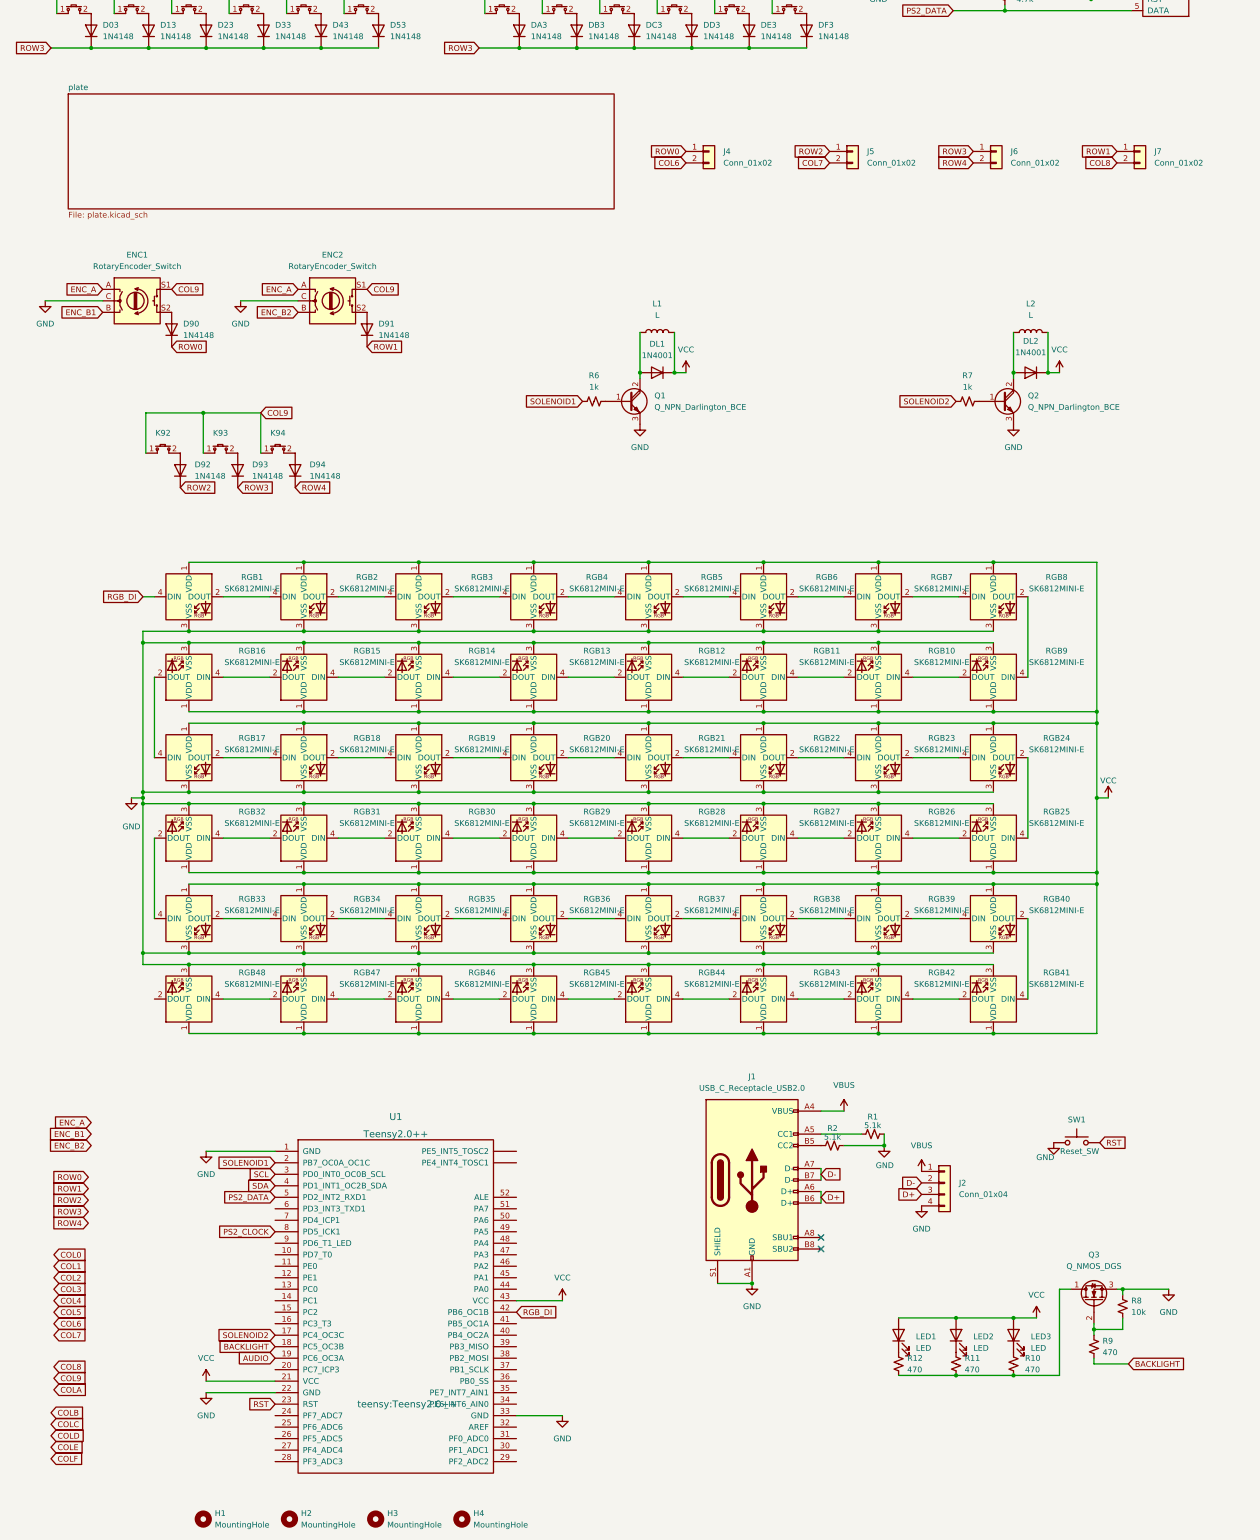
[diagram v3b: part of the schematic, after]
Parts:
- removed D60, D61, D62, D63, D64, D70, D71, D72, D73, D80, D81, D82, D83, D84: 1N4148, Diode_SMD:D_SOD-123, symbol Diode:1N4148
- removed DIP1: DS04-254-1L-04BK, DS04-254-1L-04BK:SW_DS04-254-1L-04BK, symbol DS04-254-1L-04BK:DS04-254-1L-04BK
- removed H5: MountingHole, User:Trackpoint_Mounting_Holes, symbol Mechanical:MountingHole
- removed NAV1, NAV2: JOYSTICK_MINI, Sparkfun_Switches:JOYSTICK_MINI, symbol Sparkfun_Switches:JOYSTICK_MINI
- added J4, J5, J6, J7: Conn_01x02, Connector_PinHeader_2.54mm:PinHeader_1x02_P2.54mm_Vertical, symbol Connector_Generic:Conn_01x02
- H1: footprint User:MountingHole_2.4mm_M2 -> User:GH60_Top_Left_Hole
- H2: footprint User:MountingHole_2.4mm_M2 -> User:GH60_Top_Right_Hole
- H3, H4: footprint User:MountingHole_2.4mm_M2 -> User:GH60_Side_Hole
- J2: footprint (none) -> Connector_PinSocket_2.54mm:PinSocket_1x04_P2.54mm_Vertical
- SW1: footprint truckpoint:CK_RKB2_Switch -> User:Panasonic_EVPAW
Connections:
- net COL6: now also J4.2 (Pin_2)
- net COL7: now also J5.2 (Pin_2)
- net COL8: now also J7.2 (Pin_2)
- net ROW0: now also J4.1 (Pin_1)
- net ROW1: now also J7.1 (Pin_1)
- net ROW2: now also J5.1 (Pin_1)
- net ROW3: now also J6.1 (Pin_1)
- net ROW4: now also J6.2 (Pin_2)
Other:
- added sheet plate (plate.kicad_sch)
